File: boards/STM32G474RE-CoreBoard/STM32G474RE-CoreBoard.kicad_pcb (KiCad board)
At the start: 4 copper layers, 70 x 70 mm, 37 parts, among them J1 USB-C, J2 PORT_L, J3 PORT_B, J4 PORT_R, J5 PORT_T, J6 DEBUG, SW1 RESET, SW2 BOOT0, U1 STM32G474RET6, U2 AP2112K-3.3, Y1 8MHz, Y2 32.768kHz

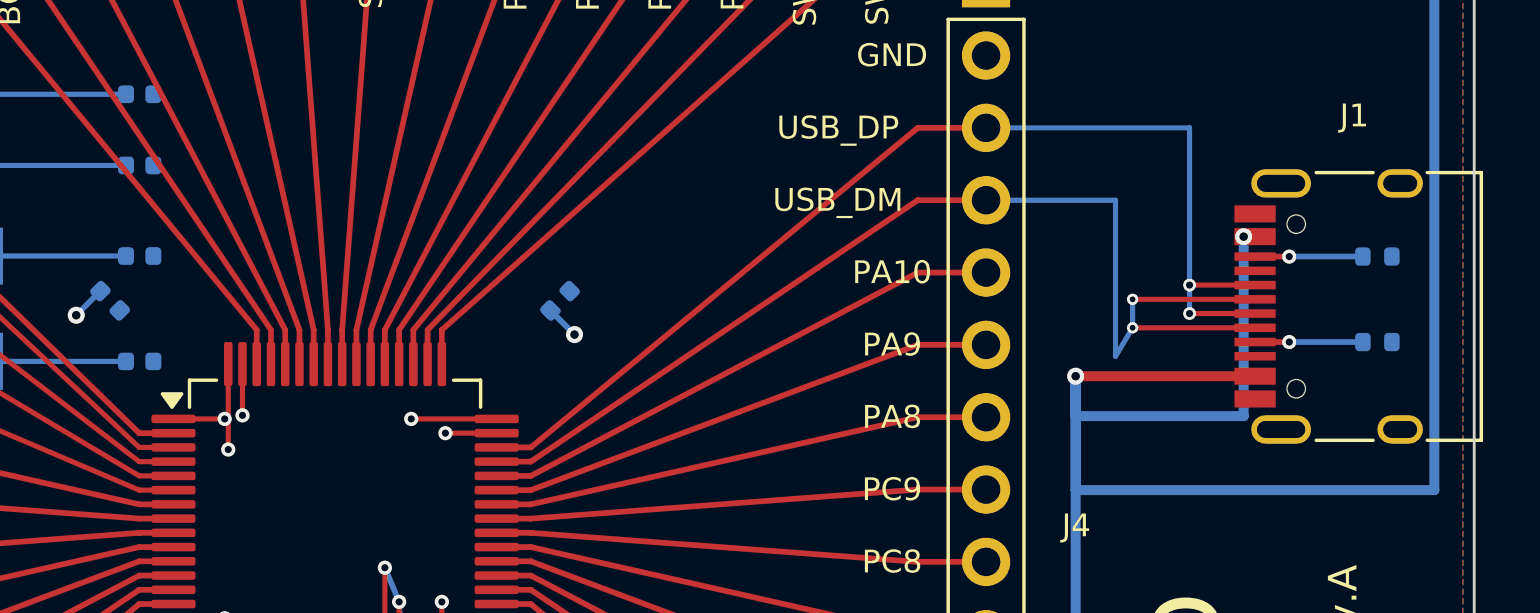
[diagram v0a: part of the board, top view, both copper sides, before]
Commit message: Устранить замечания DRC KiCad на плате G474
- Правило зазора в проекте приведено к 0.15 мм: плата разводилась под
  него, а KiCad ставил по умолчанию 0.2 и помечал 23 нормальных места
  как ошибки. Предел JLCPCB для этого процесса - 0.09 мм.
- via VBAT (вывод 1) уехала на 0.137 мм от via GND вывода 63:
  укорочен отвод с 1.8 до 1.35 мм.
- via USB_DM были 0.40/0.20 мм - ниже собственных правил платы,
  приведены к 0.45/0.25 мм.
- Земляные пады USB-C цеплялись к полигону одной перемычкой вместо
  двух: переведены на сплошное соединение.
- Убрана шелкография J1, выходившая за контур платы.

Co-Authored-By: Claude Opus 5 <noreply@anthropic.com>
Claude-Session: https://claude.ai/code/session_014TdfexXmnKj4uq4WkX48Er
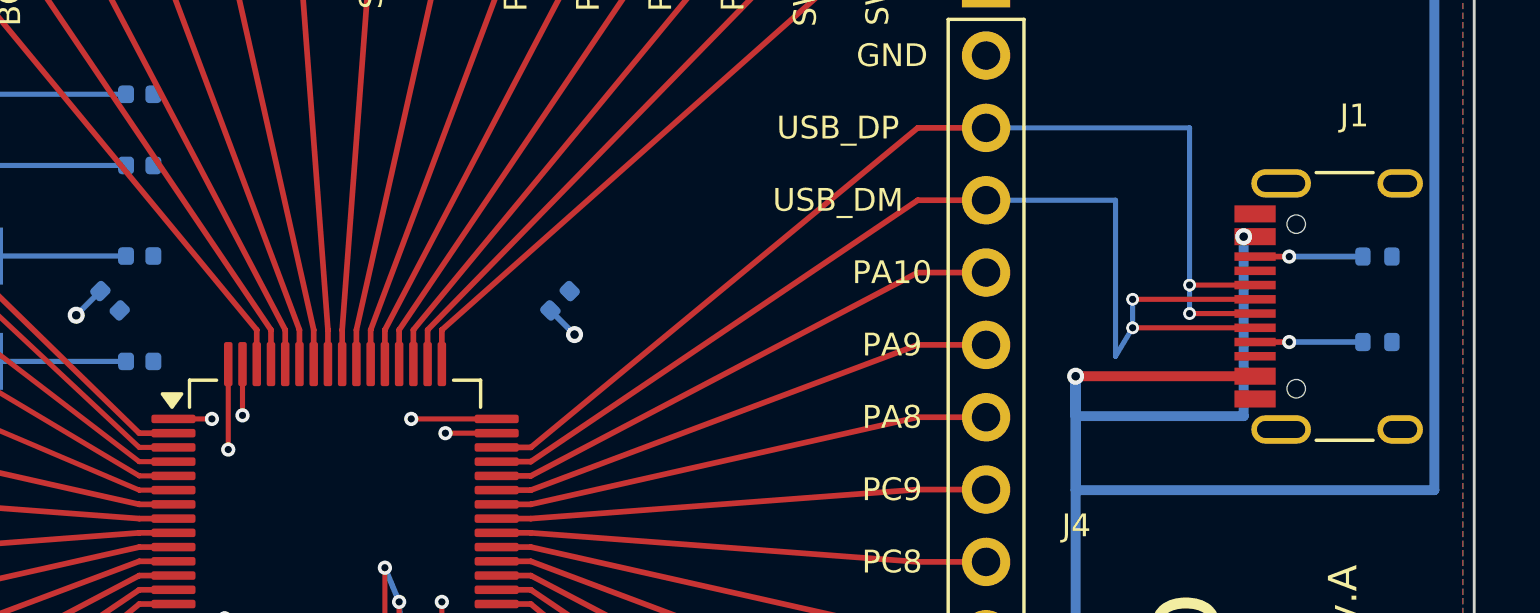
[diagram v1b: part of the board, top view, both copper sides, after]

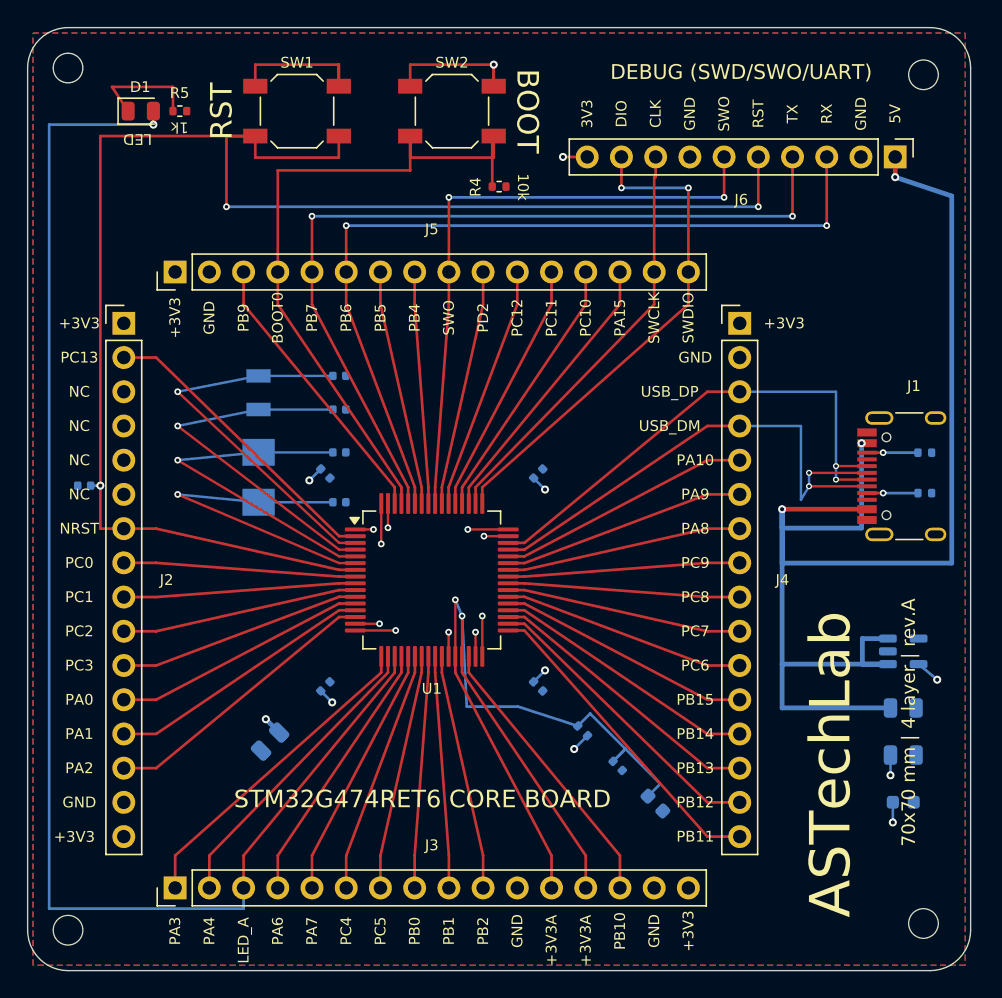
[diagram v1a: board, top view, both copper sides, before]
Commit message: Довести G474 до чистого DRC KiCad при штатных 0.2 мм
Раньше плата разводилась под 0.15 мм и правило проекта подгонялось под
геометрию. Теперь наоборот - геометрия приведена к стандартным 0.2 мм,
правило вернулось к значению по умолчанию.

- сигнальные дорожки 0.2 -> 0.15 мм: при шаге выводов LQFP64 0.5 мм
  ширина 0.2 не оставляла 0.2 мм зазора в расходящемся веере
- USB D+/D- 0.18 -> 0.14 мм: via D+ проходила в 0.185 мм от дорожки D-
- via земли внутри корпуса смещены перпендикулярно от вывода питания
  своей пары, отвод идёт сперва прямо внутрь и лишь потом наискось
- верхняя via VBUS отодвинута от земляного пада USB-C

Заодно закрыты замечания сверки платы со схемой:
- футпринтам проставлено имя библиотеки в FPID
- значения D1 и R3 приведены к схемным (LED, 0R/FB); на шелке у R3
  по-прежнему короткое 0R
- монтажные отверстия H1-H4 добавлены в схему

Проверка: зазоры 0 нарушений при 0.2 мм, несоединённых 0, courtyard 0,
шелкография 0, hole-to-hole минимум 0.716 мм.

Co-Authored-By: Claude Opus 5 <noreply@anthropic.com>
Claude-Session: https://claude.ai/code/session_014TdfexXmnKj4uq4WkX48Er
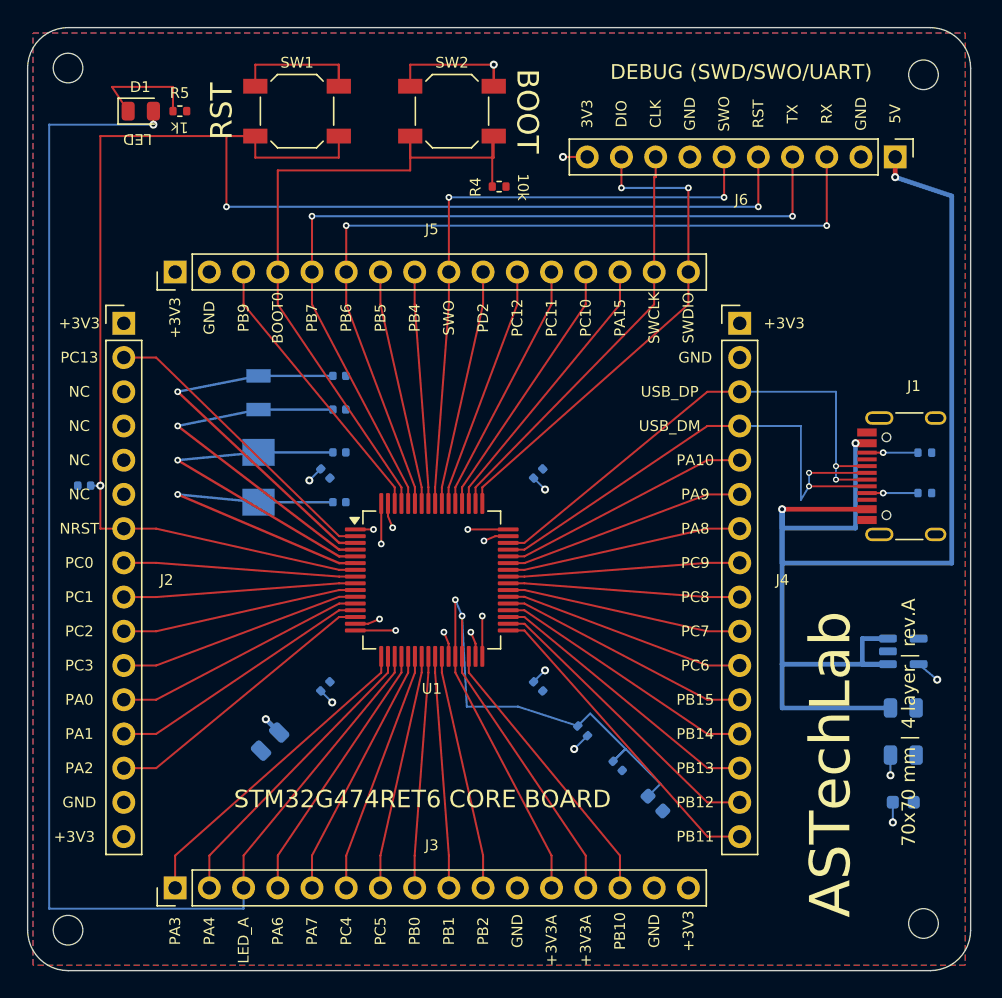
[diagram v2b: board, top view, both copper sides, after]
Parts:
- C1, C13, C14, C15, C16, C17, C2, C3, C4, C9: footprint C_0402_1005Metric -> Capacitor_SMD:C_0402_1005Metric
- C10, C6: footprint C_0603_1608Metric -> Capacitor_SMD:C_0603_1608Metric
- C5, C7, C8: footprint C_0805_2012Metric -> Capacitor_SMD:C_0805_2012Metric
- D1: value USER -> LED; footprint LED_0805_2012Metric -> LED_SMD:LED_0805_2012Metric
- H1, H2, H3, H4: footprint MountingHole_2.2mm_M2 -> MountingHole:MountingHole_2.2mm_M2
- J1: footprint USB_C_Receptacle_HRO_TYPE-C-31-M-12 -> Connector_USB:USB_C_Receptacle_HRO_TYPE-C-31-M-12
- J2, J3, J4, J5: footprint PinHeader_1x16_P2.54mm_Vertical -> Connector_PinHeader_2.54mm:PinHeader_1x16_P2.54mm_Vertical
- J6: footprint PinHeader_1x10_P2.54mm_Vertical -> Connector_PinHeader_2.54mm:PinHeader_1x10_P2.54mm_Vertical
- R1, R2, R3, R4, R5: footprint R_0402_1005Metric -> Resistor_SMD:R_0402_1005Metric
- SW1, SW2: footprint SW_SPST_SKQG_WithoutStem -> Button_Switch_SMD:SW_SPST_SKQG_WithoutStem
- U1: footprint LQFP-64_10x10mm_P0.5mm -> Package_QFP:LQFP-64_10x10mm_P0.5mm
- U2: footprint SOT-23-5 -> Package_TO_SOT_SMD:SOT-23-5
- Y1: footprint Crystal_SMD_5032-2Pin_5.0x3.2mm -> Crystal:Crystal_SMD_5032-2Pin_5.0x3.2mm
- Y2: footprint Crystal_SMD_MicroCrystal_CC7V-T1A-2Pin_3.2x1.5mm -> Crystal:Crystal_SMD_MicroCrystal_CC7V-T1A-2Pin_3.2x1.5mm

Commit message: Перевести проект на собственную библиотеку футпринтов
KiCad сверяет футпринты платы с библиотечными, а системные библиотеки
меняются от версии к версии: KiCad 10 у пользователя давал 31
предупреждение lib_footprint_mismatch против копий из KiCad 7.

Генератор теперь выгружает все 14 использованных футпринтов в
auto_probe.pretty рядом с платой и прописывает fp-lib-table. Плата и
схема ссылаются на эту библиотеку. Копии снимаются уже после всех
доработок, поэтому в них попадает и сплошное соединение земли USB-C,
и снятая с края шелкография, и подменённая 3D-модель.

Побочный эффект - проект перестал зависеть от системных библиотек
KiCad вообще: собирается одинаково у любого, кто его клонирует.

Co-Authored-By: Claude Opus 5 <noreply@anthropic.com>
Claude-Session: https://claude.ai/code/session_014TdfexXmnKj4uq4WkX48Er
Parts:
- C1, C13, C14, C15, C16, C17, C2, C3, C4, C9: footprint Capacitor_SMD:C_0402_1005Metric -> auto_probe:C_0402_1005Metric
- C10, C6: footprint Capacitor_SMD:C_0603_1608Metric -> auto_probe:C_0603_1608Metric
- C5, C7, C8: footprint Capacitor_SMD:C_0805_2012Metric -> auto_probe:C_0805_2012Metric
- D1: footprint LED_SMD:LED_0805_2012Metric -> auto_probe:LED_0805_2012Metric
- H1, H2, H3, H4: footprint MountingHole:MountingHole_2.2mm_M2 -> auto_probe:MountingHole_2.2mm_M2
- J1: footprint Connector_USB:USB_C_Receptacle_HRO_TYPE-C-31-M-12 -> auto_probe:USB_C_Receptacle_HRO_TYPE-C-31-M-12
- J2, J3, J4, J5: footprint Connector_PinHeader_2.54mm:PinHeader_1x16_P2.54mm_Vertical -> auto_probe:PinHeader_1x16_P2.54mm_Vertical
- J6: footprint Connector_PinHeader_2.54mm:PinHeader_1x10_P2.54mm_Vertical -> auto_probe:PinHeader_1x10_P2.54mm_Vertical
- R1, R2, R3, R4, R5: footprint Resistor_SMD:R_0402_1005Metric -> auto_probe:R_0402_1005Metric
- SW1, SW2: footprint Button_Switch_SMD:SW_SPST_SKQG_WithoutStem -> auto_probe:SW_SPST_SKQG_WithoutStem
- U1: footprint Package_QFP:LQFP-64_10x10mm_P0.5mm -> auto_probe:LQFP-64_10x10mm_P0.5mm
- U2: footprint Package_TO_SOT_SMD:SOT-23-5 -> auto_probe:SOT-23-5
- Y1: footprint Crystal:Crystal_SMD_5032-2Pin_5.0x3.2mm -> auto_probe:Crystal_SMD_5032-2Pin_5.0x3.2mm
- Y2: footprint Crystal:Crystal_SMD_MicroCrystal_CC7V-T1A-2Pin_3.2x1.5mm -> auto_probe:Crystal_SMD_MicroCrystal_CC7V-T1A-2Pin_3.2x1.5mm

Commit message: G474: подготовка к заказу JLCPCB - кварцы под склад, легенда на шелкографии
Кварцы подобраны по наличию: HSE 8 МГц X50328MSB2GI (C115962, Basic, CL 20 пФ)
с обвязкой 33 пФ (C1562, Basic) вместо 12 пФ; LSE остался C97606 (CL 12.5 пФ),
обвязка 6.8 пФ -> 18 пФ как на H723. Номиналы исправлены в схеме, плате и на
шелкографии, цепи не менялись.

Шелкография: номиналы у деталей заменены легендой на нижней стороне (стиль
H723, компактнее), у компонентов остались только обозначения; четыре рефа
раздвинуты от падов.

Генератор:
- ROT_FIX в export.py теперь по имени корпуса, а не по рефу (LQFP -90,
  SOT-23-8 +180 - проверено заказами H723 и CAN-Unit);
- примечания о нагрузочной ёмкости кварцев - по номиналу (CL_NOTE),
  новые номера LCSC: 33 пФ, 120R, TCAN332G, MSK12C02;
- паяные перемычки (SolderJumper) исключаются из BOM.

H723: выходные файлы перегенерированы, содержимое эквивалентно.

Co-Authored-By: Claude Fable 5 <noreply@anthropic.com>
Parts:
- C13, C14: value 12pF -> 33pF
- C15, C16: value 6.8pF -> 18pF
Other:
- board text added: "C1-C4,C6,C9,C17 100nF"
- board text added: "C10 1uF"
- board text added: "C13,C14 33pF"
- board text added: "C15,C16 18pF"
- board text added: "C5 4.7uF"
- board text added: "C7,C8 10uF"
- board text added: "R1,R2 5.1k"
- board text added: "R3 0R/FB"
- board text added: "R4 10k"
- board text added: "R5 1k"
- board text added: "U2 AP2112K-3.3 D1 LED"
- board text added: "Y1 8MHz"
- board text added: "Y2 32.768kHz"
- board text removed: "0R"
- board text removed: "100nF"
- board text removed: "10k"
- board text removed: "10uF"
- board text removed: "12pF"
- board text removed: "1k"
- board text removed: "1uF"
- board text removed: "32.768kHz"
- board text removed: "4.7uF"
- board text removed: "5.1k"
- board text removed: "6.8pF"
- board text removed: "8MHz"
- board text removed: "AP2112K-3.3"
- board text removed: "LED"
